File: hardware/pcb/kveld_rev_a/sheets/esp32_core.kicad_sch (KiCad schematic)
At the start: 28 parts, among them J4 TC2030 recovery pads, SW1 CATEGORY KSC321GLFS, SW2 NEXT KSC321GLFS, U1 ESP32-S3-WROOM-1-N16 / WROOM-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

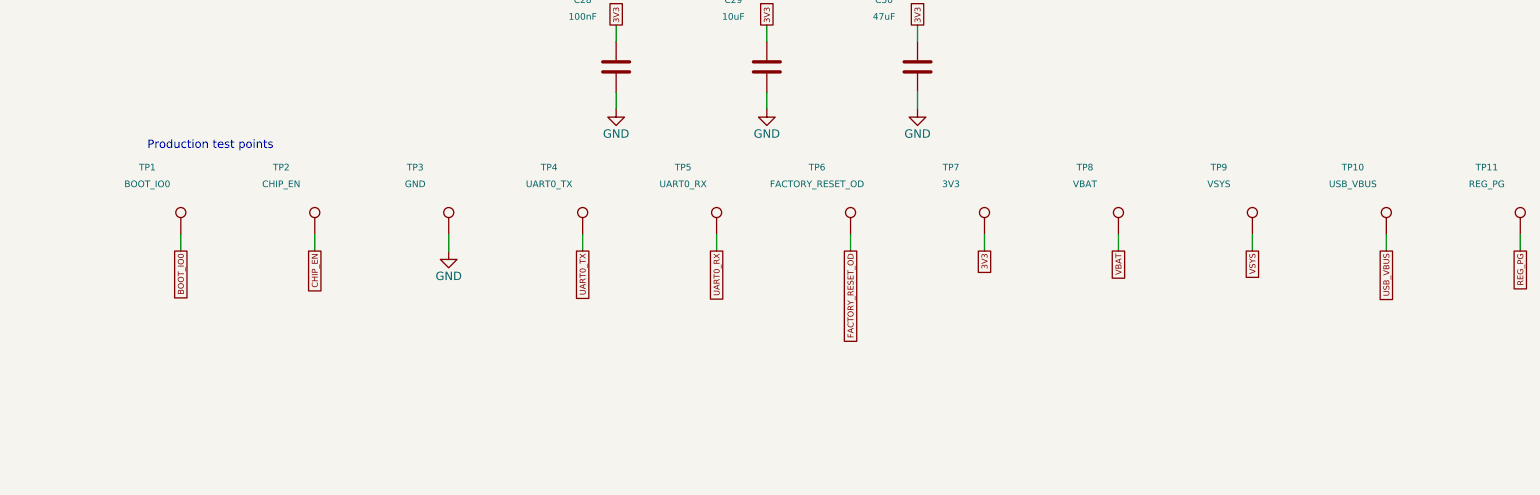
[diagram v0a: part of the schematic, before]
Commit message: fix(hw): correct rev A charger/regulator wiring and assign footprints
Two schematic errors that ERC could not catch, both electrically valid
but topologically wrong:

- TPS63802 feedback divider was shorted: a straight wire tied FB to VOUT
  and bypassed R14, so the part would regulate the 3.3 V rail down to its
  0.5 V reference. Rewired VOUT -> R14 -> FB node -> R15 -> GND (3.31 V).
- BQ25185 TS/MR and the pack NTC wire (J3.2) were tied to VBAT, which the
  charger reads as an out-of-range temperature and suspends charging.
  TS/MR is now the BATT_NTC net carrying only J3.2; BAT stays on VBAT.
  The 38 uA TS source and the 10 kOhm B=3435 pack NTC to GND need no
  external bias (~1.5 C / ~59 C window).

Footprints: every symbol now carries one. SW1/SW2 use the KiCad
CK_KSC6xxG land (matches the KSC3 drawing). Four parts with no library
match get project land patterns in kveld.pretty (registered via
fp-lib-table): Texas_DLA0010A_VSON-HR-10 (no exposed pad), L_Coilcraft_
XFL4015, L_TDK_VLS4012, and a preliminary LED_Kingbright_APBA2006 whose
pad numbers follow the LED_Dual_AAKK symbol.

Also regroup TP1-TP11 from a full-width row into a compact two-row block,
and ignore the KiCad Local-History plugin's nested git repo.

ERC, constraint-board DRC, BOM and STEP export still pass.

Co-Authored-By: Claude Opus 4.8 <noreply@anthropic.com>
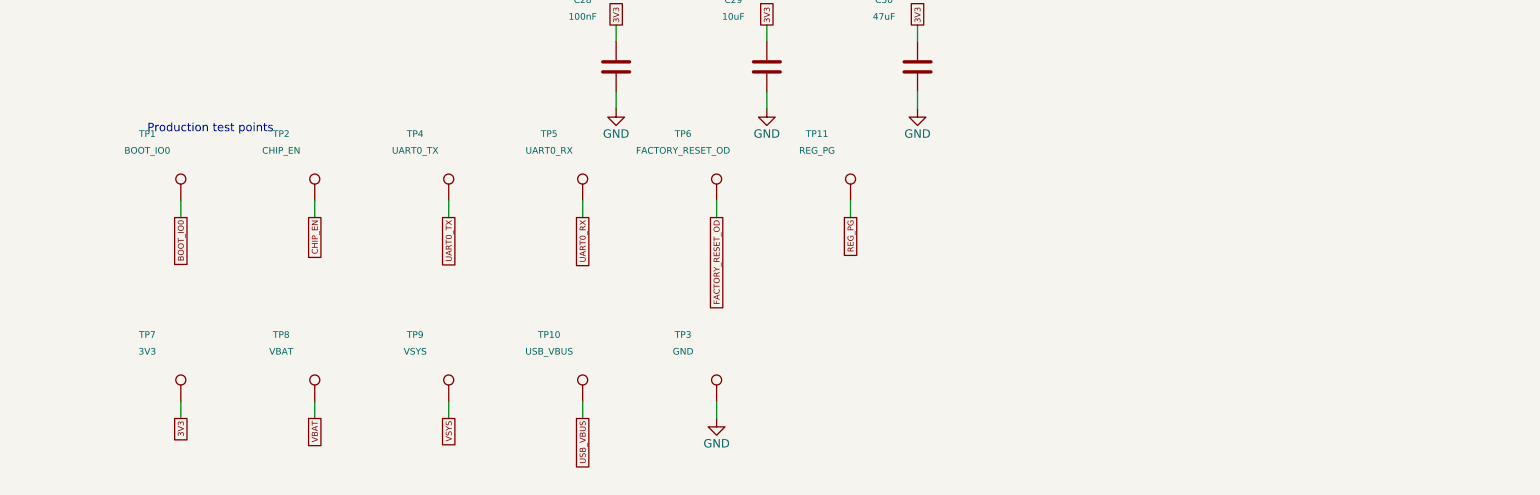
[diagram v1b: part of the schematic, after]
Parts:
- D4: footprint (none) -> kveld:LED_Kingbright_APBA2006SURKCGKC
- SW1, SW2: footprint (none) -> Button_Switch_SMD:SW_Push_1P1T_NO_CK_KSC6xxG
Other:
- moved on the sheet: TP1, TP10, TP11, TP2, TP3, TP4, TP5, TP6, TP7, TP8, TP9
